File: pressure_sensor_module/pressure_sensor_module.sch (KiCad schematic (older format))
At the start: 2 parts

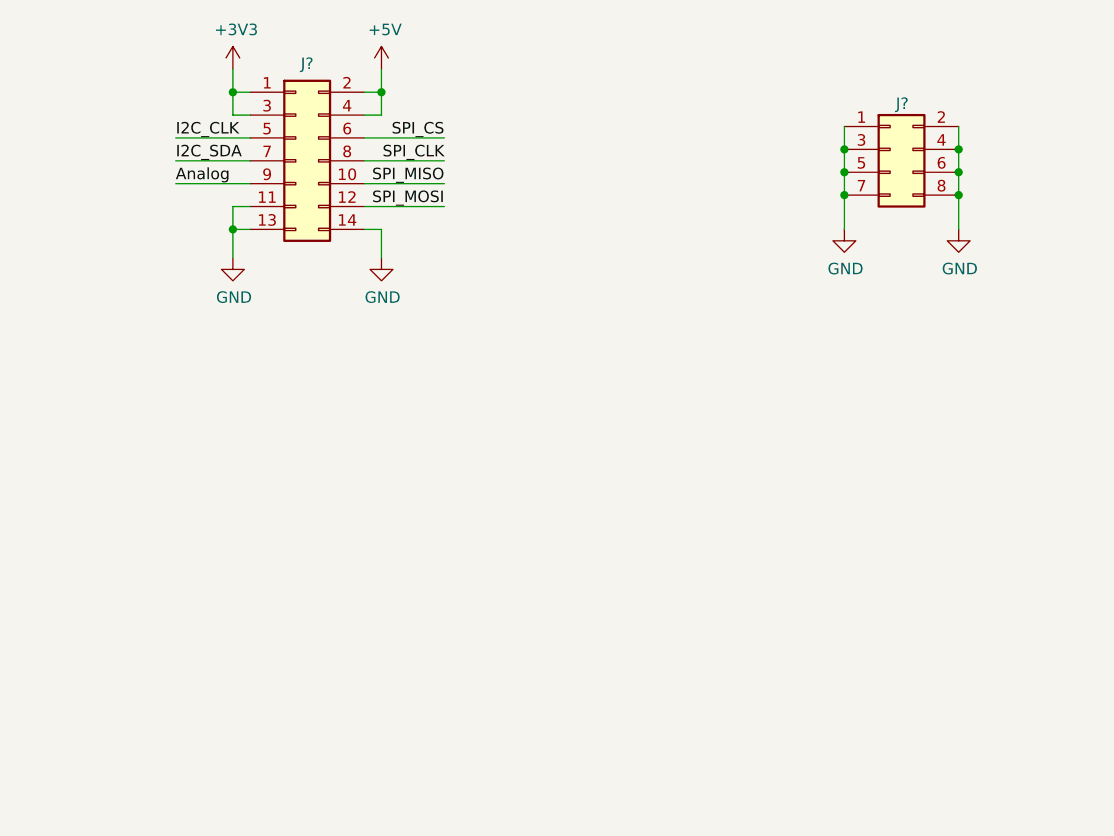
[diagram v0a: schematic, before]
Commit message: - Added Sensor_pressure library - Added 3d shape for MPX5100 sensor - MPX5100 footprint created - Connections on SEEschema for presure_sensor_module - Connections on PCBnew for pressure_sensor_module
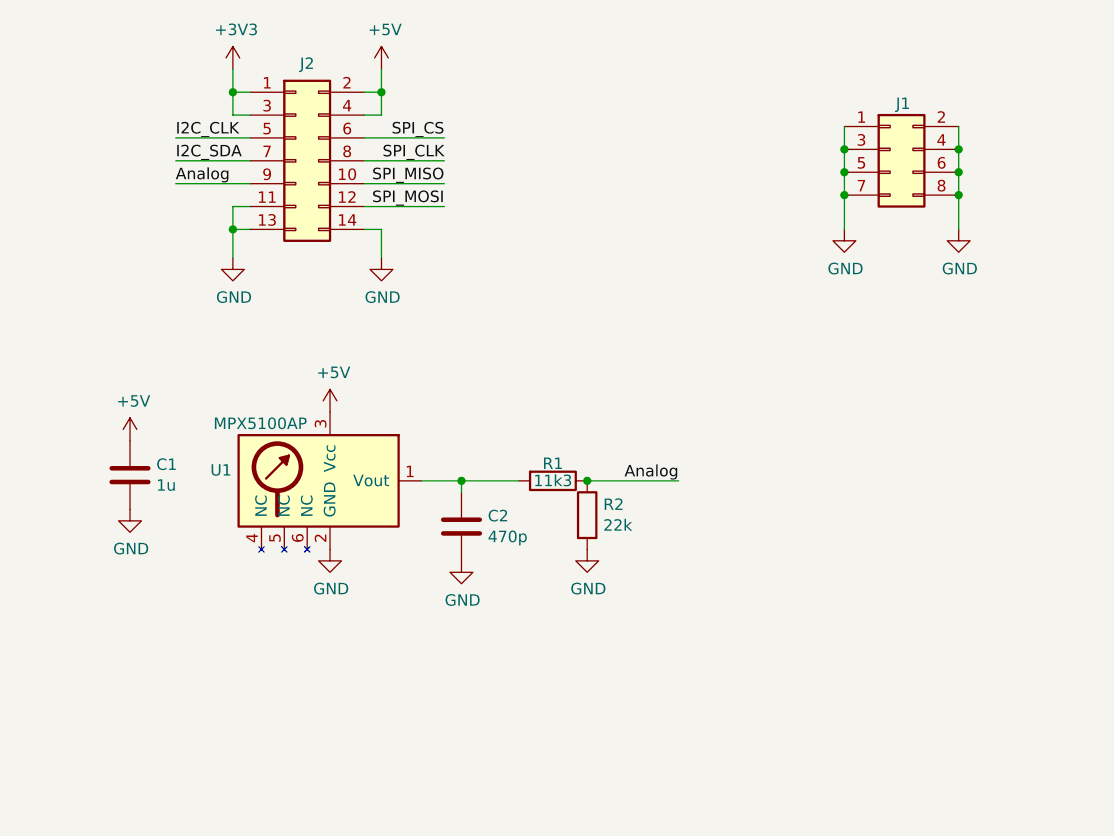
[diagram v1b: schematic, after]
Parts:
- added C1: 1u, Capacitor_SMD:C_0603_1608Metric, symbol Device:C
- added C2: 470p, Capacitor_SMD:C_0603_1608Metric, symbol Device:C
- added R1: 11k3, Resistor_SMD:R_0603_1608Metric, symbol Device:R
- added R2: 22k, Resistor_SMD:R_0603_1608Metric, symbol Device:R
- added U1: MPX5100AP, TH_project:MPX5100, symbol Sensor_Pressure:MPX5100AP
- J1: renamed from J?; footprint (none) -> Connector_PinHeader_2.54mm:PinHeader_2x04_P2.54mm_Vertical
- J2: renamed from J?; footprint (none) -> Connector_PinHeader_2.54mm:PinHeader_2x07_P2.54mm_Vertical
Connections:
- net +5V: now also C1.1, U1.3 (Vcc)
- net Analog: now also R1.1, R2.1
- net GND: now also C1.2, C2.2, R2.2, U1.2 (GND)
- new net: C2.1, R1.2, U1.1 (Vout)
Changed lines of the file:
@@
 $EndDescr
 $Comp
-L Connector_Generic:Conn_02x04_Odd_Even J?
+L Connector_Generic:Conn_02x04_Odd_Even J1
 U 1 1 5EF3F442
 P 4950 1825
-F 0 "J?" H 4975 2025 50  0000 L CNN
+F 0 "J1" H 4975 2025 50  0000 L CNN
 F 1 "Conn_02x04_Odd_Even" V 5045 2005 50  0001 L CNN
-F 2 "" H 4950 1825 50  0001 C CNN
+F 2 "Connector_PinHeader_2.54mm:PinHeader_2x04_P2.54mm_Vertical" H 4950 1825 50  0001 C CNN
 F 3 "~" H 4950 1825 50  0001 C CNN
 	1    4950 1825
@@
 $EndComp
 $Comp
-L Connector_Generic:Conn_02x07_Odd_Even J?
+L Connector_Generic:Conn_02x07_Odd_Even J2
 U 1 1 5EF420CD
 P 2350 1875
-F 0 "J?" H 2400 2300 50  0000 C CNN
+F 0 "J2" H 2400 2300 50  0000 C CNN
 F 1 "Conn_02x07_Odd_Even" H 2400 2301 50  0001 C CNN
-F 2 "" H 2350 1875 50  0001 C CNN
+F 2 "Connector_PinHeader_2.54mm:PinHeader_2x07_P2.54mm_Vertical" H 2350 1875 50  0001 C CNN
 F 3 "~" H 2350 1875 50  0001 C CNN
 	1    2350 1875
@@
 $EndComp
 $Comp
-L power:GND #PWR?
+L power:GND #PWR03
 U 1 1 5EF42DC4
 P 4750 2175
-F 0 "#PWR?" H 4750 1925 50  0001 C CNN
+F 0 "#PWR03" H 4750 1925 50  0001 C CNN
 F 1 "GND" H 4755 2002 50  0000 C CNN
 F 2 "" H 4750 2175 50  0001 C CNN
@@
 $EndComp
 $Comp
-L power:GND #PWR?
+L power:GND #PWR04
 U 1 1 5EF7B615
 P 5250 2175
-F 0 "#PWR?" H 5250 1925 50  0001 C CNN
+F 0 "#PWR04" H 5250 1925 50  0001 C CNN
 F 1 "GND" H 5255 2002 50  0000 C CNN
 F 2 "" H 5250 2175 50  0001 C CNN
@@
 Connection ~ 5250 1825
 $Comp
-L power:+3V3 #PWR?
+L power:+3V3 #PWR01
 U 1 1 5EF7D25A
 P 2075 1475
-F 0 "#PWR?" H 2075 1325 50  0001 C CNN
+F 0 "#PWR01" H 2075 1325 50  0001 C CNN
 F 1 "+3V3" H 2090 1648 50  0000 C CNN
 F 2 "" H 2075 1475 50  0001 C CNN
@@
 $EndComp
 $Comp
-L power:+5V #PWR?
+L power:+5V #PWR02
 U 1 1 5EF7DBDC
 P 2725 1475
-F 0 "#PWR?" H 2725 1325 50  0001 C CNN
+F 0 "#PWR02" H 2725 1325 50  0001 C CNN
 F 1 "+5V" H 2740 1648 50  0000 C CNN
 F 2 "" H 2725 1475 50  0001 C CNN
@@
 Connection ~ 2725 1575
 $Comp
-L power:GND #PWR?
+L power:GND #PWR05
 U 1 1 5EF7EBAB
 P 2075 2300
-F 0 "#PWR?" H 2075 2050 50  0001 C CNN
+F 0 "#PWR05" H 2075 2050 50  0001 C CNN
 F 1 "GND" H 2080 2127 50  0000 C CNN
 F 2 "" H 2075 2300 50  0001 C CNN
@@
 $EndComp
 $Comp
-L power:GND #PWR?
+L power:GND #PWR06
 U 1 1 5EF7F0CC
 P 2725 2300
-F 0 "#PWR?" H 2725 2050 50  0001 C CNN
+F 0 "#PWR06" H 2725 2050 50  0001 C CNN
 F 1 "GND" H 2730 2127 50  0000 C CNN
 F 2 "" H 2725 2300 50  0001 C CNN
@@
 Text Label 1825 1975 0    50   ~ 0
 Analog
+$Comp
+L Sensor_Pressure:MPX5100AP U1
+U 1 1 5EF424A1
+P 2500 3275
+F 0 "U1" H 2070 3321 50  0000 R CNN
+F 1 "MPX5100AP" H 2400 3525 50  0000 R CNN
+F 2 "TH_project:MPX5100" H 2000 2925 50  0001 C CNN
+F 3 "" H 2500 3875 50  0001 C CNN
+	1    2500 3275
+	1    0    0    -1
+$EndComp
+$Comp
+L power:+5V #PWR07
+U 1 1 5EF4409E
+P 2500 2975
+F 0 "#PWR07" H 2500 2825 50  0001 C CNN
+F 1 "+5V" H 2515 3148 50  0000 C CNN
+F 2 "" H 2500 2975 50  0001 C CNN
+F 3 "" H 2500 2975 50  0001 C CNN
+	1    2500 2975
+	1    0    0    -1
+$EndComp
+$Comp
+L power:GND #PWR010
+U 1 1 5EF44CF8
+P 2500 3575
+F 0 "#PWR010" H 2500 3325 50  0001 C CNN
+F 1 "GND" H 2505 3402 50  0000 C CNN
+F 2 "" H 2500 3575 50  0001 C CNN
+F 3 "" H 2500 3575 50  0001 C CNN
+	1    2500 3575
+	1    0    0    -1
+$EndComp
+$Comp
+L Device:R R1
+U 1 1 5EF4514E
+P 3475 3275
+F 0 "R1" V 3400 3275 50  0000 C CNN
+F 1 "11k3" V 3475 3275 50  0000 C CNN
+F 2 "Resistor_SMD:R_0603_1608Metric" V 3405 3275 50  0001 C CNN
+F 3 "~" H 3475 3275 50  0001 C CNN
+F 4 "A102208CT-ND" V 3475 3275 50  0001 C CNN "DigiKey"
+	1    3475 3275
+	0    1    1    0
+$EndComp
+$Comp
+L Device:R R2
+U 1 1 5EF45EC3
+P 3625 3425
+F 0 "R2" H 3695 3471 50  0000 L CNN
+F 1 "22k" H 3695 3380 50  0000 L CNN
+F 2 "Resistor_SMD:R_0603_1608Metric" V 3555 3425 50  0001 C CNN
+F 3 "~" H 3625 3425 50  0001 C CNN
+F 4 "A103066CT-ND" H 3625 3425 50  0001 C CNN "DigiKey"
+	1    3625 3425
+	1    0    0    -1
+$EndComp
+$Comp
+L power:GND #PWR011
+U 1 1 5EF462A2
+P 3625 3575
+F 0 "#PWR011" H 3625 3325 50  0001 C CNN
+F 1 "GND" H 3630 3402 50  0000 C CNN
+F 2 "" H 3625 3575 50  0001 C CNN
+F 3 "" H 3625 3575 50  0001 C CNN
+	1    3625 3575
+	1    0    0    -1
+$EndComp
+Wire Wire Line
+	3625 3275 4025 3275
+Connection ~ 3625 3275
+Text Label 4025 3275 2    50   ~ 0
+Analog
+$Comp
+L Device:C C1
+U 1 1 5EF4B509
+P 1625 3250
+F 0 "C1" H 1740 3296 50  0000 L CNN
+F 1 "1u" H 1740 3205 50  0000 L CNN
+F 2 "Capacitor_SMD:C_0603_1608Metric" H 1663 3100 50  0001 C CNN
+F 3 "~" H 1625 3250 50  0001 C CNN
+	1    1625 3250
+	1    0    0    -1
+$EndComp
+$Comp
+L power:+5V #PWR08
+U 1 1 5EF4D69E
+P 1625 3100
+F 0 "#PWR08" H 1625 2950 50  0001 C CNN
+F 1 "+5V" H 1640 3273 50  0000 C CNN
+F 2 "" H 1625 3100 50  0001 C CNN
+F 3 "" H 1625 3100 50  0001 C CNN
+	1    1625 3100
+	1    0    0    -1
+$EndComp
+$Comp
+L power:GND #PWR09
+U 1 1 5EF4DF5A
+P 1625 3400
+F 0 "#PWR09" H 1625 3150 50  0001 C CNN
+F 1 "GND" H 1630 3227 50  0000 C CNN
+F 2 "" H 1625 3400 50  0001 C CNN
+F 3 "" H 1625 3400 50  0001 C CNN
+	1    1625 3400
+	1    0    0    -1
+$EndComp
+$Comp
+L Device:C C2
+U 1 1 5EF4E99C
+P 3075 3475
+F 0 "C2" H 3190 3521 50  0000 L CNN
+F 1 "470p" H 3190 3430 50  0000 L CNN
+F 2 "Capacitor_SMD:C_0603_1608Metric" H 3113 3325 50  0001 C CNN
+F 3 "~" H 3075 3475 50  0001 C CNN
+	1    3075 3475
+	1    0    0    -1
+$EndComp
+$Comp
+L power:GND #PWR012
+U 1 1 5EF50C28
+P 3075 3625
+F 0 "#PWR012" H 3075 3375 50  0001 C CNN
+F 1 "GND" H 3080 3452 50  0000 C CNN
+F 2 "" H 3075 3625 50  0001 C CNN
+F 3 "" H 3075 3625 50  0001 C CNN
+	1    3075 3625
+	1    0    0    -1
+$EndComp
+Wire Wire Line
+	2900 3275 3075 3275
+Wire Wire Line
+	3075 3325 3075 3275
+Connection ~ 3075 3275
+Wire Wire Line
+	3075 3275 3325 3275
 $EndSCHEMATC

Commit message: - Added footprint MPX100 vertical - Modified pinHeader footprints to SMD
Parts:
- J1: footprint Connector_PinHeader_2.54mm:PinHeader_2x04_P2.54mm_Vertical -> Connector_PinHeader_2.54mm:PinHeader_2x04_P2.54mm_Vertical_SMD
- J2: footprint Connector_PinHeader_2.54mm:PinHeader_2x07_P2.54mm_Vertical -> Connector_PinHeader_2.54mm:PinHeader_2x07_P2.54mm_Vertical_SMD
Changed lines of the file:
@@
 F 0 "J1" H 4975 2025 50  0000 L CNN
 F 1 "Conn_02x04_Odd_Even" V 5045 2005 50  0001 L CNN
-F 2 "Connector_PinHeader_2.54mm:PinHeader_2x04_P2.54mm_Vertical" H 4950 1825 50  0001 C CNN
+F 2 "Connector_PinHeader_2.54mm:PinHeader_2x04_P2.54mm_Vertical_SMD" H 4950 1825 50  0001 C CNN
 F 3 "~" H 4950 1825 50  0001 C CNN
 	1    4950 1825
@@
 F 0 "J2" H 2400 2300 50  0000 C CNN
 F 1 "Conn_02x07_Odd_Even" H 2400 2301 50  0001 C CNN
-F 2 "Connector_PinHeader_2.54mm:PinHeader_2x07_P2.54mm_Vertical" H 2350 1875 50  0001 C CNN
+F 2 "Connector_PinHeader_2.54mm:PinHeader_2x07_P2.54mm_Vertical_SMD" H 2350 1875 50  0001 C CNN
 F 3 "~" H 2350 1875 50  0001 C CNN
 	1    2350 1875

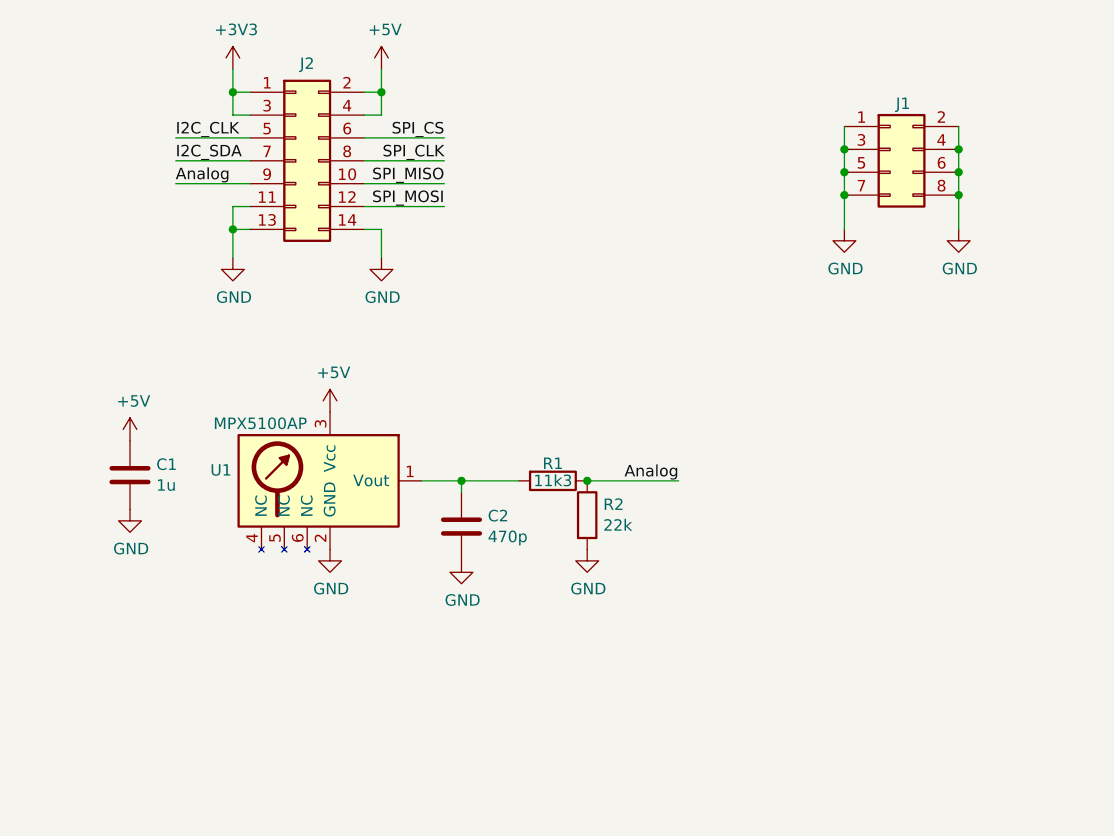
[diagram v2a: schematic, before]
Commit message: added an LM358 to improve possible problems with impedance between the sensor and the STM
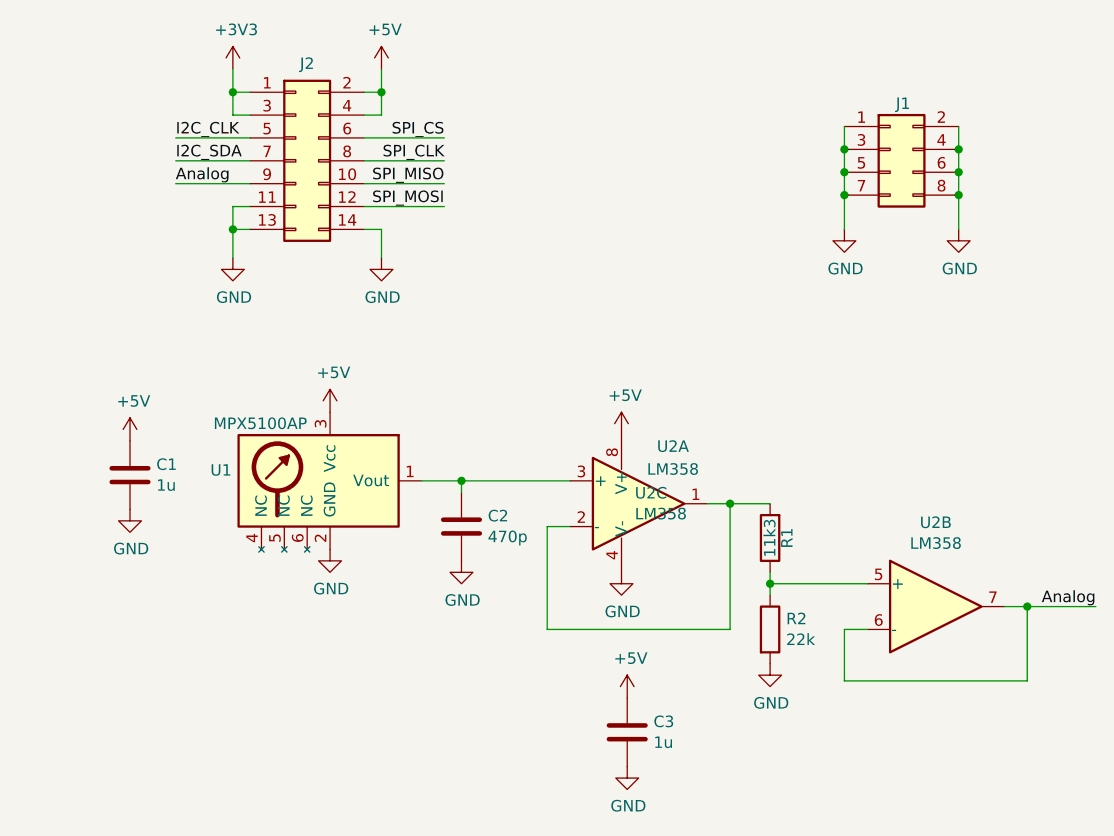
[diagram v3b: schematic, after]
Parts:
- added C3: 1u, Capacitor_SMD:C_0603_1608Metric, symbol Device:C
- added U2: LM358, Package_SO:TSSOP-8_4.4x3mm_P0.65mm, symbol Amplifier_Operational:LM358
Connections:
- net +5V: now also C3.1, U2.8 (V+)
- net Analog: now also U2.6 (-), U2.7; no longer R1.1, R2.1
- net GND: now also C3.2, U2.4 (V-)
- net at C2.1, U1.1 (Vout): now also U2.3 (+); no longer R1.2
- new net: R1.1, R2.1, U2.5 (+)
- new net: R1.2, U2.1, U2.2 (-)
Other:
- moved on the sheet: R1, R2
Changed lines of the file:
@@
 L Device:R R1
 U 1 1 5EF4514E
-P 3475 3275
-F 0 "R1" V 3400 3275 50  0000 C CNN
-F 1 "11k3" V 3475 3275 50  0000 C CNN
-F 2 "Resistor_SMD:R_0603_1608Metric" V 3405 3275 50  0001 C CNN
-F 3 "~" H 3475 3275 50  0001 C CNN
-F 4 "A102208CT-ND" V 3475 3275 50  0001 C CNN "DigiKey"
-	1    3475 3275
-	0    1    1    0
+P 4425 3525
+F 0 "R1" V 4350 3525 50  0000 C CNN
+F 1 "11k3" V 4425 3525 50  0000 C CNN
+F 2 "Resistor_SMD:R_0603_1608Metric" V 4355 3525 50  0001 C CNN
+F 3 "~" H 4425 3525 50  0001 C CNN
+F 4 "A102208CT-ND" V 4425 3525 50  0001 C CNN "DigiKey"
+	1    4425 3525
+	-1   0    0    1
 $EndComp
 $Comp
 L Device:R R2
 U 1 1 5EF45EC3
-P 3625 3425
-F 0 "R2" H 3695 3471 50  0000 L CNN
-F 1 "22k" H 3695 3380 50  0000 L CNN
-F 2 "Resistor_SMD:R_0603_1608Metric" V 3555 3425 50  0001 C CNN
-F 3 "~" H 3625 3425 50  0001 C CNN
-F 4 "A103066CT-ND" H 3625 3425 50  0001 C CNN "DigiKey"
-	1    3625 3425
+P 4425 3925
+F 0 "R2" H 4495 3971 50  0000 L CNN
+F 1 "22k" H 4495 3880 50  0000 L CNN
+F 2 "Resistor_SMD:R_0603_1608Metric" V 4355 3925 50  0001 C CNN
+F 3 "~" H 4425 3925 50  0001 C CNN
+F 4 "A103066CT-ND" H 4425 3925 50  0001 C CNN "DigiKey"
+	1    4425 3925
 	1    0    0    -1
 $EndComp
@@
 L power:GND #PWR011
 U 1 1 5EF462A2
-P 3625 3575
-F 0 "#PWR011" H 3625 3325 50  0001 C CNN
-F 1 "GND" H 3630 3402 50  0000 C CNN
-F 2 "" H 3625 3575 50  0001 C CNN
-F 3 "" H 3625 3575 50  0001 C CNN
-	1    3625 3575
-	1    0    0    -1
-$EndComp
-Wire Wire Line
-	3625 3275 4025 3275
-Connection ~ 3625 3275
-Text Label 4025 3275 2    50   ~ 0
+P 4425 4075
+F 0 "#PWR011" H 4425 3825 50  0001 C CNN
+F 1 "GND" H 4430 3902 50  0000 C CNN
+F 2 "" H 4425 4075 50  0001 C CNN
+F 3 "" H 4425 4075 50  0001 C CNN
+	1    4425 4075
+	1    0    0    -1
+$EndComp
+Wire Wire Line
+	5450 3825 5550 3825
+Text Label 5850 3825 2    50   ~ 0
 Analog
 $Comp
@@
 	3075 3325 3075 3275
 Connection ~ 3075 3275
-Wire Wire Line
-	3075 3275 3325 3275
+$Comp
+L Amplifier_Operational:LM358 U2
+U 1 1 5EFE46C6
+P 3850 3375
+F 0 "U2" H 4000 3625 50  0000 C CNN
+F 1 "LM358" H 4000 3525 50  0000 C CNN
+F 2 "Package_SO:TSSOP-8_4.4x3mm_P0.65mm" H 3850 3375 50  0001 C CNN
+F 3 "http://www.ti.com/lit/ds/symlink/lm2904-n.pdf" H 3850 3375 50  0001 C CNN
+F 4 "296-51268-1-ND" H 3850 3375 50  0001 C CNN "DigiKey"
+	1    3850 3375
+	1    0    0    -1
+$EndComp
+$Comp
+L Amplifier_Operational:LM358 U2
+U 2 1 5EFE985C
+P 5150 3825
+F 0 "U2" H 5150 4192 50  0000 C CNN
+F 1 "LM358" H 5150 4101 50  0000 C CNN
+F 2 "Package_SO:TSSOP-8_4.4x3mm_P0.65mm" H 5150 3825 50  0001 C CNN
+F 3 "http://www.ti.com/lit/ds/symlink/lm2904-n.pdf" H 5150 3825 50  0001 C CNN
+F 4 "296-51268-1-ND" H 5150 3825 50  0001 C CNN "DigiKey"
+	2    5150 3825
+	1    0    0    -1
+$EndComp
+$Comp
+L Amplifier_Operational:LM358 U2
+U 3 1 5EFEB94D
+P 3875 3375
+F 0 "U2" H 3833 3421 50  0000 L CNN
+F 1 "LM358" H 3833 3330 50  0000 L CNN
+F 2 "" H 3875 3375 50  0001 C CNN
+F 3 "http://www.ti.com/lit/ds/symlink/lm2904-n.pdf" H 3875 3375 50  0001 C CNN
+	3    3875 3375
+	1    0    0    -1
+$EndComp
+Wire Wire Line
+	3075 3275 3550 3275
+Wire Wire Line
+	3550 3475 3450 3475
+Wire Wire Line
+	3450 3475 3450 3925
+Wire Wire Line
+	3450 3925 4250 3925
+Wire Wire Line
+	4250 3925 4250 3375
+Wire Wire Line
+	4250 3375 4150 3375
+Wire Wire Line
+	4425 3375 4250 3375
+Connection ~ 4250 3375
+Wire Wire Line
+	4425 3775 4425 3725
+Wire Wire Line
+	4425 3725 4850 3725
+Connection ~ 4425 3725
+Wire Wire Line
+	4425 3725 4425 3675
+Wire Wire Line
+	4850 3925 4750 3925
+Wire Wire Line
+	4750 3925 4750 4150
+Wire Wire Line
+	4750 4150 5550 4150
+Wire Wire Line
+	5550 4150 5550 3825
+Connection ~ 5550 3825
+Wire Wire Line
+	5550 3825 5850 3825
+$Comp
+L power:+5V #PWR013
+U 1 1 5F01629C
+P 3775 3075
+F 0 "#PWR013" H 3775 2925 50  0001 C CNN
+F 1 "+5V" H 3790 3248 50  0000 C CNN
+F 2 "" H 3775 3075 50  0001 C CNN
+F 3 "" H 3775 3075 50  0001 C CNN
+	1    3775 3075
+	1    0    0    -1
+$EndComp
+$Comp
+L power:GND #PWR014
+U 1 1 5F016CC2
+P 3775 3675
+F 0 "#PWR014" H 3775 3425 50  0001 C CNN
+F 1 "GND" H 3780 3502 50  0000 C CNN
+F 2 "" H 3775 3675 50  0001 C CNN
+F 3 "" H 3775 3675 50  0001 C CNN
+	1    3775 3675
+	1    0    0    -1
+$EndComp
+$Comp
+L Device:C C3
+U 1 1 5F018655
+P 3800 4375
+F 0 "C3" H 3915 4421 50  0000 L CNN
+F 1 "1u" H 3915 4330 50  0000 L CNN
+F 2 "Capacitor_SMD:C_0603_1608Metric" H 3838 4225 50  0001 C CNN
+F 3 "~" H 3800 4375 50  0001 C CNN
+	1    3800 4375
+	1    0    0    -1
+$EndComp
+$Comp
+L power:+5V #PWR015
+U 1 1 5F01865F
+P 3800 4225
+F 0 "#PWR015" H 3800 4075 50  0001 C CNN
+F 1 "+5V" H 3815 4398 50  0000 C CNN
+F 2 "" H 3800 4225 50  0001 C CNN
+F 3 "" H 3800 4225 50  0001 C CNN
+	1    3800 4225
+	1    0    0    -1
+$EndComp
+$Comp
+L power:GND #PWR016
+U 1 1 5F018669
+P 3800 4525
+F 0 "#PWR016" H 3800 4275 50  0001 C CNN
+F 1 "GND" H 3805 4352 50  0000 C CNN
+F 2 "" H 3800 4525 50  0001 C CNN
+F 3 "" H 3800 4525 50  0001 C CNN
+	1    3800 4525
+	1    0    0    -1
+$EndComp
 $EndSCHEMATC

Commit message: Added DigiKey parts number
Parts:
- C1, C3: DigiKey (none) -> 1276-1182-1-ND
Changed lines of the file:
@@
 F 2 "Capacitor_SMD:C_0603_1608Metric" H 1663 3100 50  0001 C CNN
 F 3 "~" H 1625 3250 50  0001 C CNN
+F 4 "1276-1182-1-ND" H 1625 3250 50  0001 C CNN "DigiKey"
 	1    1625 3250
 	1    0    0    -1
@@
 F 2 "Capacitor_SMD:C_0603_1608Metric" H 3838 4225 50  0001 C CNN
 F 3 "~" H 3800 4375 50  0001 C CNN
+F 4 "1276-1182-1-ND" H 3800 4375 50  0001 C CNN "DigiKey"
 	1    3800 4375
 	1    0    0    -1
